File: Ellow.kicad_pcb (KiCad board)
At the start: 2 copper layers, 46 parts, among them J2 686116183422, J3 Conn_01x02_Female, Q1 A03407, Q2 A03407, SW9 RotaryEncoder_Switch, U1 AP2112K-3.3

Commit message: saved
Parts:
- added J1: USB_C_Receptacle_USB2.0, Connector_USB:USB_C_Receptacle_HRO_TYPE-C-31-M-12, F.Cu at (237.5, 92.7)
- added J4: Bus_M.2_Socket_A, ellow:M_2_EdgeConnector, F.Cu at (224.8, 102.9)
- added U2: E73-2G4M08S1C, ellow:E73-2G4M08S1C-52840, F.Cu at (237.5, 116.8)
- moved D1 23.6 mm to (163.8, 99.1)
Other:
- board outline added: 21 x 30 mm

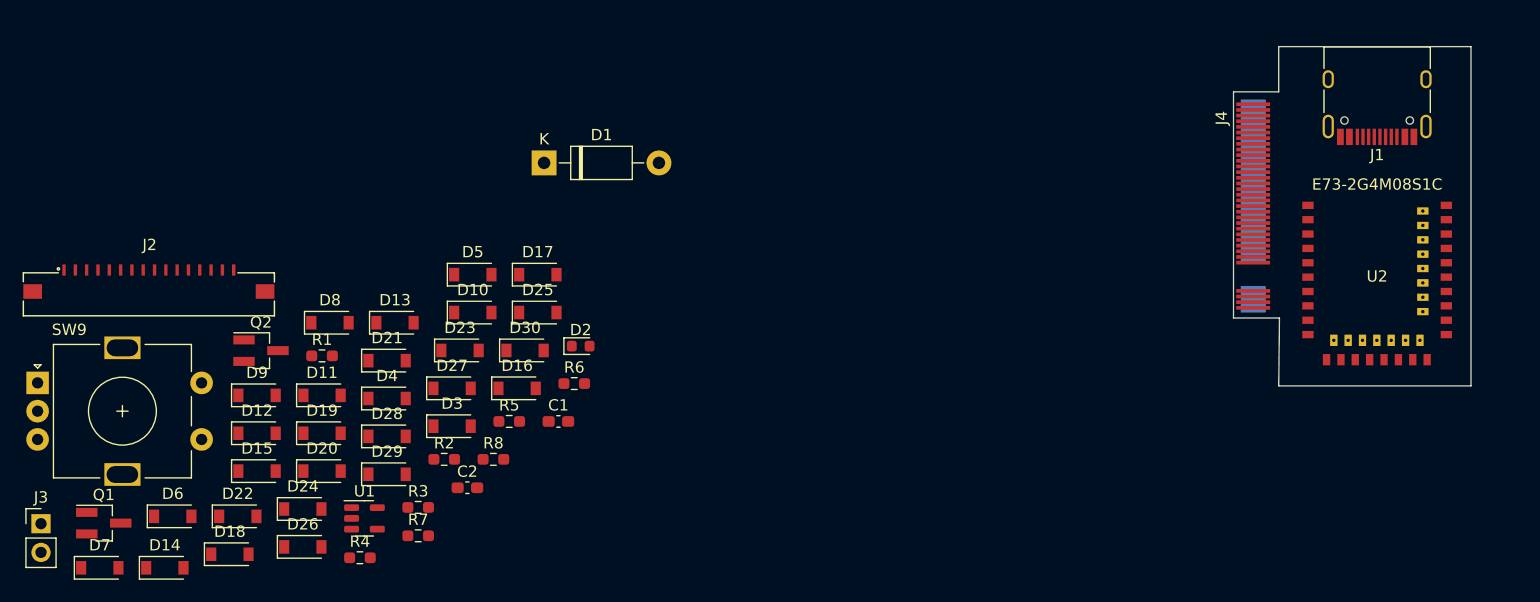
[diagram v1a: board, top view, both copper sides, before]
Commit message: moved shield stuff to another board
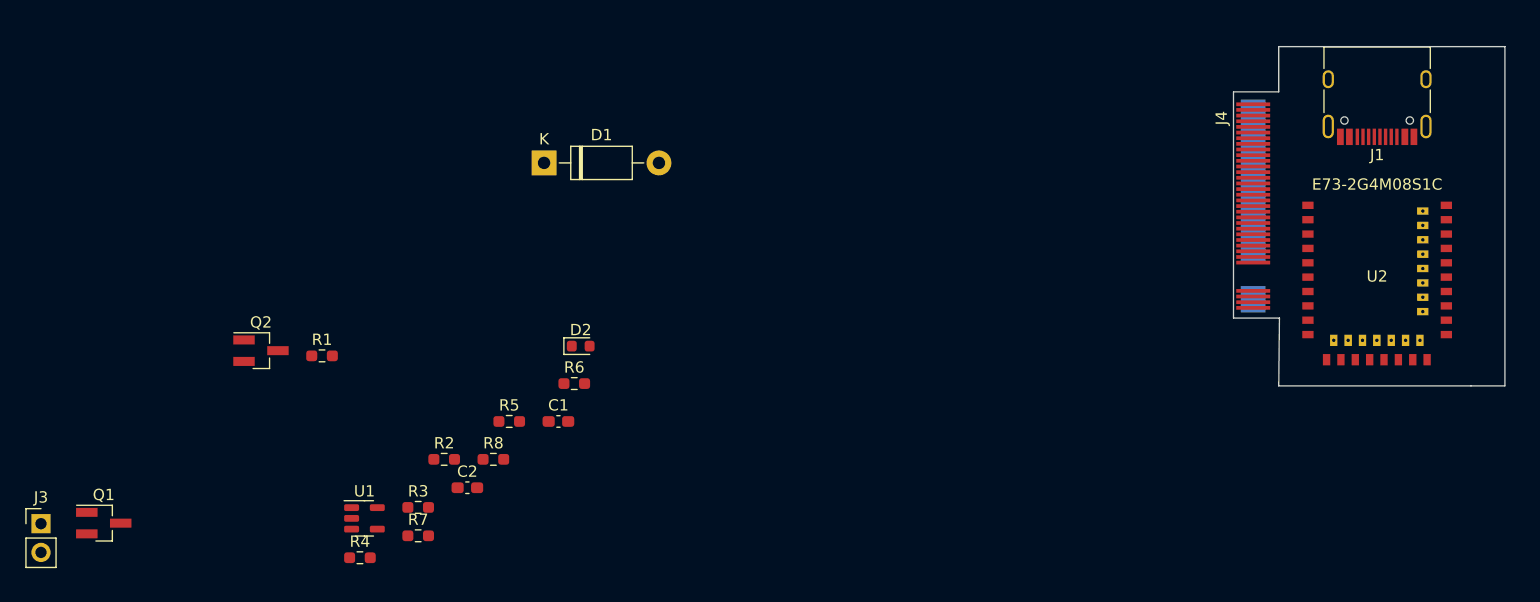
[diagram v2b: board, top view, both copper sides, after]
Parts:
- removed D10, D11, D12, D13, D14, D15, D16, D17, D18, D19, D20, D21, D22, D23, D24, D25, D26, D27, D28, D29, D3, D30, D4, D5, D6, D7, D8, D9: D_Small, Diode_SMD:D_SOD-123
- removed J2: 686116183422, 686116183422:686116183422
- removed SW9: RotaryEncoder_Switch, Rotary_Encoder:RotaryEncoder_Alps_EC11E-Switch_Vertical_H20mm
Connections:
- J4 pad 1: Net-(J4-Pad1) -> GND
- J4 pad 18: Net-(J4-Pad1) -> GND
- J4 pad 2: Net-(J4-Pad2) -> VDD_H
- J4 pad 23: Net-(J4-Pad1) -> GND
- J4 pad 24: Net-(J4-Pad1) -> GND
- J4 pad 29: Net-(J4-Pad1) -> GND
- J4 pad 30: Net-(J4-Pad1) -> GND
- J4 pad 33: Net-(J4-Pad1) -> GND
- J4 pad 36: Net-(J4-Pad1) -> GND
- J4 pad 39: Net-(J4-Pad1) -> GND
- J4 pad 4: Net-(J4-Pad2) -> VDD_H
- J4 pad 45: Net-(J4-Pad1) -> GND
- J4 pad 51: Net-(J4-Pad1) -> GND
- J4 pad 57: Net-(J4-Pad1) -> GND
- J4 pad 69: Net-(J4-Pad1) -> GND
- J4 pad 7: Net-(J4-Pad1) -> GND
- J4 pad 72: Net-(J4-Pad2) -> VDD_H
- J4 pad 74: Net-(J4-Pad2) -> VDD_H
- J4 pad 75: Net-(J4-Pad1) -> GND
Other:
- board size 21 x 30 mm -> 24 x 30 mm

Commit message: first board for quote check. not routed
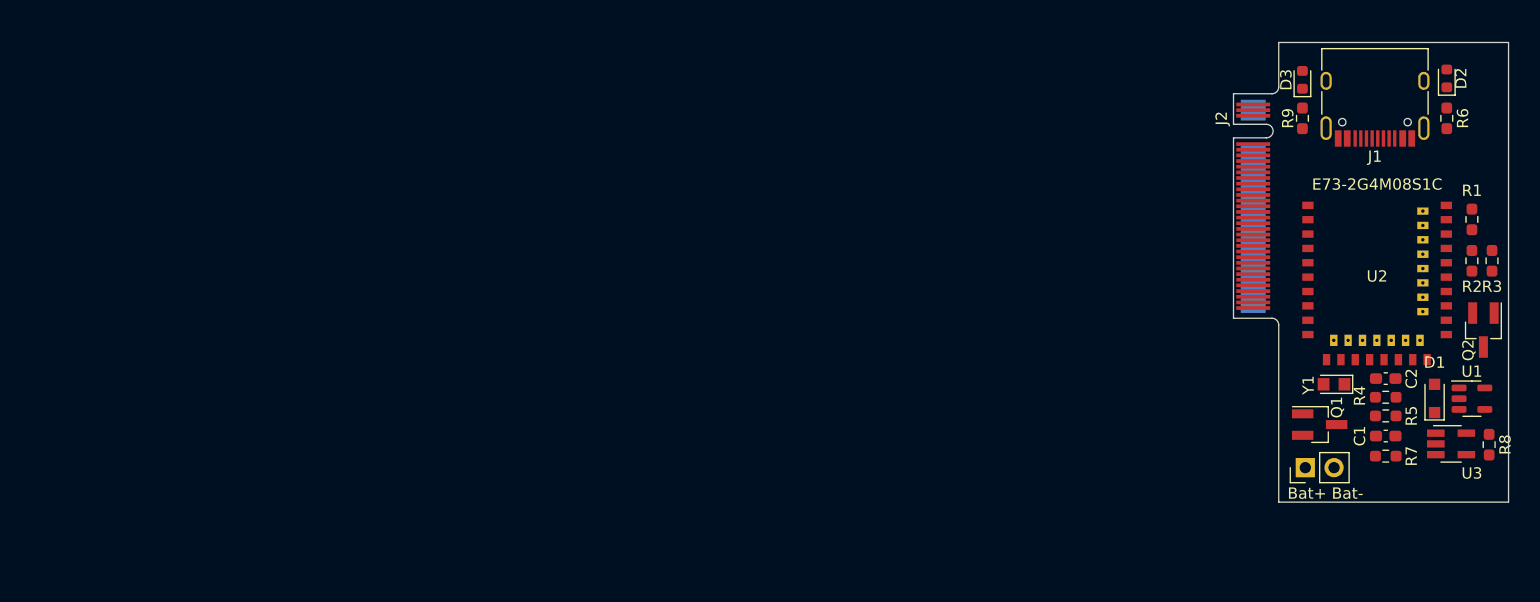
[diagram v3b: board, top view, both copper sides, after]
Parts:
- removed J4: Bus_M.2_Socket_A, ellow:M_2_EdgeConnector
- added D3: LED, LED_SMD:LED_0603_1608Metric, F.Cu at (230.9, 91.7)
- added J2: M_2_AKey_KB, ellow:M_2_EdgeConnector_A_Key, F.Cu at (224.8, 102.9)
- added R9: 10k, Resistor_SMD:R_0603_1608Metric_Pad0.98x0.95mm_HandSolder, F.Cu at (230.9, 95.1)
- added U3: LN2054Y42AMR, Package_TO_SOT_SMD:SOT-23-5_HandSoldering, F.Cu at (244.0, 123.9)
- added Y1: 32.768kHz, Crystal:Crystal_SMD_2012-2Pin_2.0x1.2mm_HandSoldering, F.Cu at (233.7, 118.6)
- Bat+ Bat-: renamed from J3
- D1: footprint Diode_THT:D_DO-41_SOD81_P10.16mm_Horizontal -> Diode_SMD:D_SOD-323_HandSoldering
- moved Bat+ Bat- 111.9 mm to (231.1, 126.0), turned to 90 degrees
- moved Q2 108.1 mm to (246.9, 113.8), turned to 270 degrees
- moved Q1 107.9 mm to (232.4, 122.2)
- moved R1 102.4 mm to (245.9, 104.1), turned to 90 degrees
- moved U1 98.5 mm to (245.9, 119.9)
- moved R3 97.4 mm to (247.7, 107.7), turned to 270 degrees
- moved R2 92.6 mm to (245.9, 107.7), turned to 90 degrees
- moved R4 91.8 mm to (238.3, 119.8), turned to 180 degrees
- moved R8 88.1 mm to (247.4, 124.0), turned to 270 degrees
- moved R7 85.8 mm to (238.3, 125.0)
- moved C2 81.8 mm to (238.3, 118.1), turned to 180 degrees
- moved D1 81.4 mm to (242.6, 119.9), turned to 90 degrees
- moved R6 80.6 mm to (243.6, 95.1), turned to 270 degrees
- moved D2 80.2 mm to (243.6, 91.6), turned to 90 degrees
- moved R5 77.5 mm to (238.3, 121.4)
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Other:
- board size 24 x 30 mm -> 24.3 x 40.6 mm

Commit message: starting to look at routing
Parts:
- added H1: MountingHole, ellow:MountingHole_M.2_3mm, F.Cu at (244.1, 107.2)
- C1: footprint Capacitor_SMD:C_0603_1608Metric_Pad1.08x0.95mm_HandSolder -> Capacitor_SMD:C_0603_1608Metric; moved to B.Cu
- C2: footprint Capacitor_SMD:C_0603_1608Metric_Pad1.08x0.95mm_HandSolder -> Capacitor_SMD:C_0603_1608Metric
- D1: footprint Diode_SMD:D_SOD-323_HandSoldering -> Diode_SMD:D_SOD-323
- J3: renamed from Bat+ Bat-; footprint Connector_PinHeader_2.54mm:PinHeader_1x02_P2.54mm_Vertical -> Connector_PinHeader_1.27mm:PinHeader_1x02_P1.27mm_Vertical
- Q1, Q2: footprint Package_TO_SOT_SMD:SOT-23_Handsoldering -> Package_TO_SOT_SMD:SOT-23
- R1, R2, R3, R8: moved to B.Cu
- U3: footprint Package_TO_SOT_SMD:SOT-23-5_HandSoldering -> Package_TO_SOT_SMD:SOT-23-5
- moved R8 28.0 mm to (233.9, 99.4), turned to 180 degrees
- moved U3 25.6 mm to (233.8, 100.5), turned to 270 degrees
- moved C1 23.7 mm to (240.8, 99.7)
- moved R7 21.5 mm to (240.8, 103.7)
- moved R3 19.8 mm to (236.0, 91.7), turned to 0 degrees
- moved U1 19.7 mm to (241.0, 100.8), turned to 90 degrees
- moved Q1 19.2 mm to (237.3, 103.7)
- moved D1 17.7 mm to (234.5, 104.2)
- moved Q2 16.7 mm to (237.4, 100.1)
- moved R2 16.3 mm to (236.0, 94.7), turned to 180 degrees
- moved R1 14.7 mm to (236.0, 93.2), turned to 0 degrees
- moved Y1 12.1 mm to (239.4, 107.9), turned to 0 degrees
- moved C2 12.1 mm to (226.8, 121.9)
- moved R5 11.7 mm to (226.9, 118.9), turned to 180 degrees
- moved R4 11.4 mm to (226.9, 120.4)
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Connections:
- net Net-(U2-Pad12) renamed P0.26
- net Net-(U2-Pad14) renamed P0.06
- net Net-(U2-Pad20) renamed P0.12
- net Net-(U2-Pad22) renamed 90.07
- net Net-(U2-Pad34) renamed P0.22
- net Net-(U2-Pad36) renamed P1.00
- net Net-(U2-Pad38) renamed P1.02
- net Net-(U2-Pad40) renamed P1.04
- J2 pad 1: (no net) -> GND
- J2 pad 16: (no net) -> P0.31
- J2 pad 17: (no net) -> P0.30
- J2 pad 18: (no net) -> Net-(J2-Pad18)
- J2 pad 19: (no net) -> Net-(J2-Pad19)
- J2 pad 2: (no net) -> EXT_VCC
- J2 pad 20: (no net) -> P0.29
- J2 pad 21: (no net) -> P0.02
- J2 pad 22: (no net) -> Net-(J2-Pad22)
- J2 pad 23: (no net) -> Net-(J2-Pad23)
- J2 pad 24: (no net) -> P1.13
- J2 pad 25: (no net) -> GND
- J2 pad 26: (no net) -> Net-(J2-Pad26)
- J2 pad 27: (no net) -> Net-(J2-Pad27)
- J2 pad 28: (no net) -> P0.03
- J2 pad 29: (no net) -> P0.28
- J2 pad 3: (no net) -> Net-(J2-Pad3)
- J2 pad 30: (no net) -> Net-(J2-Pad30)
- J2 pad 31: (no net) -> Net-(J2-Pad31)
- J2 pad 32: (no net) -> P1.11
- J2 pad 33: (no net) -> P1.06
- J2 pad 34: (no net) -> Net-(J2-Pad34)
- J2 pad 35: (no net) -> Net-(J2-Pad35)
- J2 pad 36: (no net) -> P0.10
- J2 pad 37: (no net) -> P0.09
- J2 pad 38: (no net) -> Net-(J2-Pad38)
- J2 pad 39: (no net) -> Net-(J2-Pad39)
- J2 pad 4: (no net) -> Net-(J2-Pad4)
- J2 pad 40: (no net) -> GND
- J2 pad 41: (no net) -> P0.24
- J2 pad 42: (no net) -> Net-(J2-Pad42)
- J2 pad 43: (no net) -> Net-(J2-Pad43)
- J2 pad 44: (no net) -> P0.13
- J2 pad 45: (no net) -> P0.20
- J2 pad 46: (no net) -> Net-(J2-Pad46)
- J2 pad 47: (no net) -> Net-(J2-Pad47)
- J2 pad 48: (no net) -> P0.17
- J2 pad 49: (no net) -> P0.15
- J2 pad 5: (no net) -> VBAT
- J2 pad 50: (no net) -> Net-(J2-Pad50)
- J2 pad 51: (no net) -> Net-(J2-Pad51)
- J2 pad 52: (no net) -> P0.08
- J2 pad 53: (no net) -> GND
- J2 pad 54: (no net) -> Net-(J2-Pad54)
- J2 pad 55: (no net) -> Net-(J2-Pad55)
- J2 pad 56: (no net) -> Net-(J2-Pad56)
- J2 pad 57: (no net) -> Net-(J2-Pad57)
- J2 pad 58: (no net) -> Net-(J2-Pad58)
- J2 pad 59: (no net) -> Net-(J2-Pad59)
- J2 pad 6: (no net) -> RESET
- J2 pad 60: (no net) -> Net-(J2-Pad60)
- J2 pad 61: (no net) -> Net-(J2-Pad61)
- J2 pad 62: (no net) -> Net-(J2-Pad62)
- J2 pad 63: (no net) -> Net-(J2-Pad63)
- J2 pad 64: (no net) -> Net-(J2-Pad64)
- J2 pad 65: (no net) -> Net-(J2-Pad65)
- J2 pad 66: (no net) -> DATA+
- J2 pad 67: (no net) -> DATA-
- J2 pad 68: (no net) -> Net-(J2-Pad68)
- J2 pad 69: (no net) -> Net-(J2-Pad69)
- J2 pad 7: (no net) -> Net-(J2-Pad7)
- J2 pad 70: (no net) -> SWD
- J2 pad 71: (no net) -> GND
- J2 pad 72: (no net) -> Net-(J2-Pad72)
- J2 pad 73: (no net) -> Net-(J2-Pad73)
- J2 pad 74: (no net) -> SWC
- J2 pad 75: (no net) -> VDD_H
- U2 pad 1: Net-(U2-Pad1) -> P1.11
- U2 pad 10: Net-(U2-Pad10) -> P0.30
- U2 pad 16: Net-(U2-Pad16) -> P0.08
- U2 pad 28: Net-(U2-Pad28) -> P0.15
- U2 pad 3: Net-(U2-Pad3) -> P0.03
- U2 pad 30: Net-(U2-Pad30) -> P0.17
- U2 pad 32: Net-(U2-Pad32) -> P0.20
- U2 pad 33: Net-(U2-Pad33) -> P0.13
- U2 pad 35: Net-(U2-Pad35) -> P0.24
- U2 pad 4: Net-(U2-Pad4) -> P0.28
- U2 pad 41: Net-(U2-Pad41) -> P0.09
- U2 pad 42: Net-(U2-Pad42) -> P1.06
- U2 pad 43: Net-(U2-Pad43) -> P0.10
- U2 pad 6: Net-(U2-Pad6) -> P1.13
- U2 pad 7: Net-(U2-Pad7) -> P0.02
- U2 pad 8: Net-(U2-Pad8) -> P0.29
- U2 pad 9: Net-(U2-Pad9) -> P0.31
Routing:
- added copper zone on B.Cu, net GND
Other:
- board size 24.3 x 40.6 mm -> 19.3 x 37.6 mm

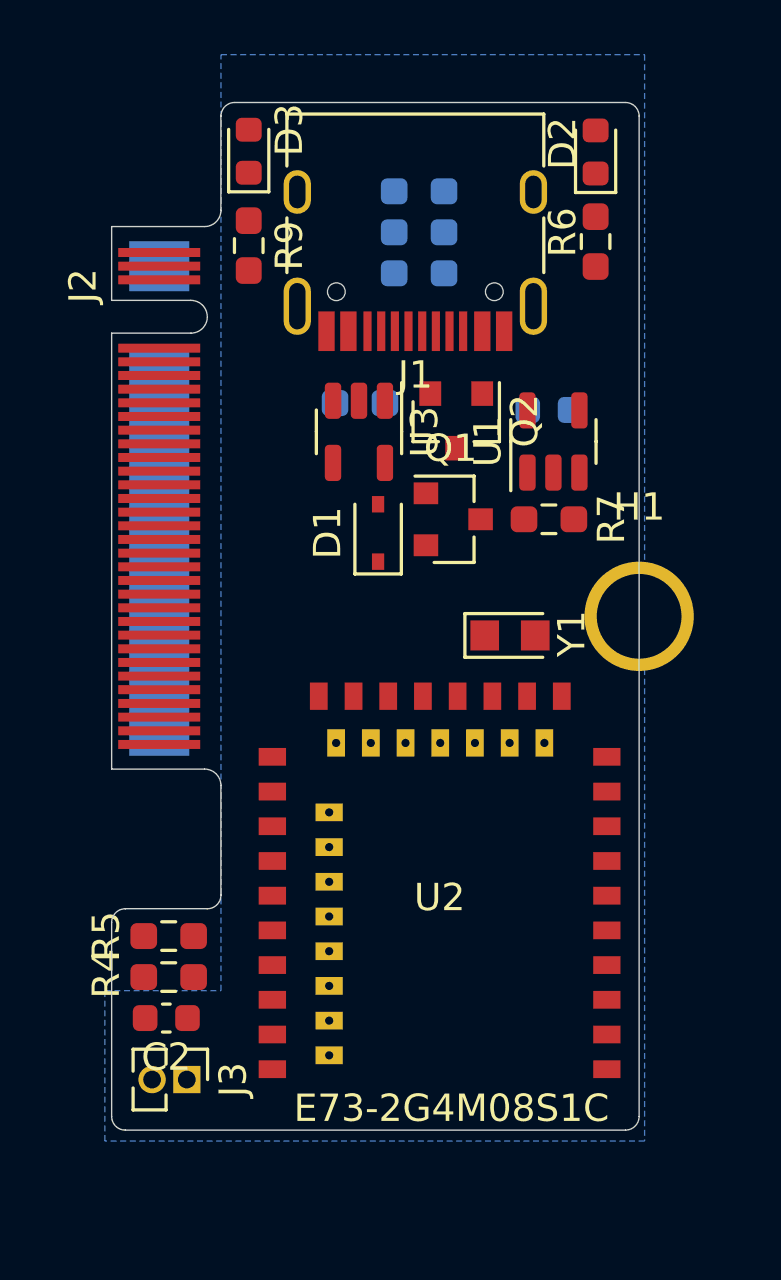
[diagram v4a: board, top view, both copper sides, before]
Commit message: no routing solution yet
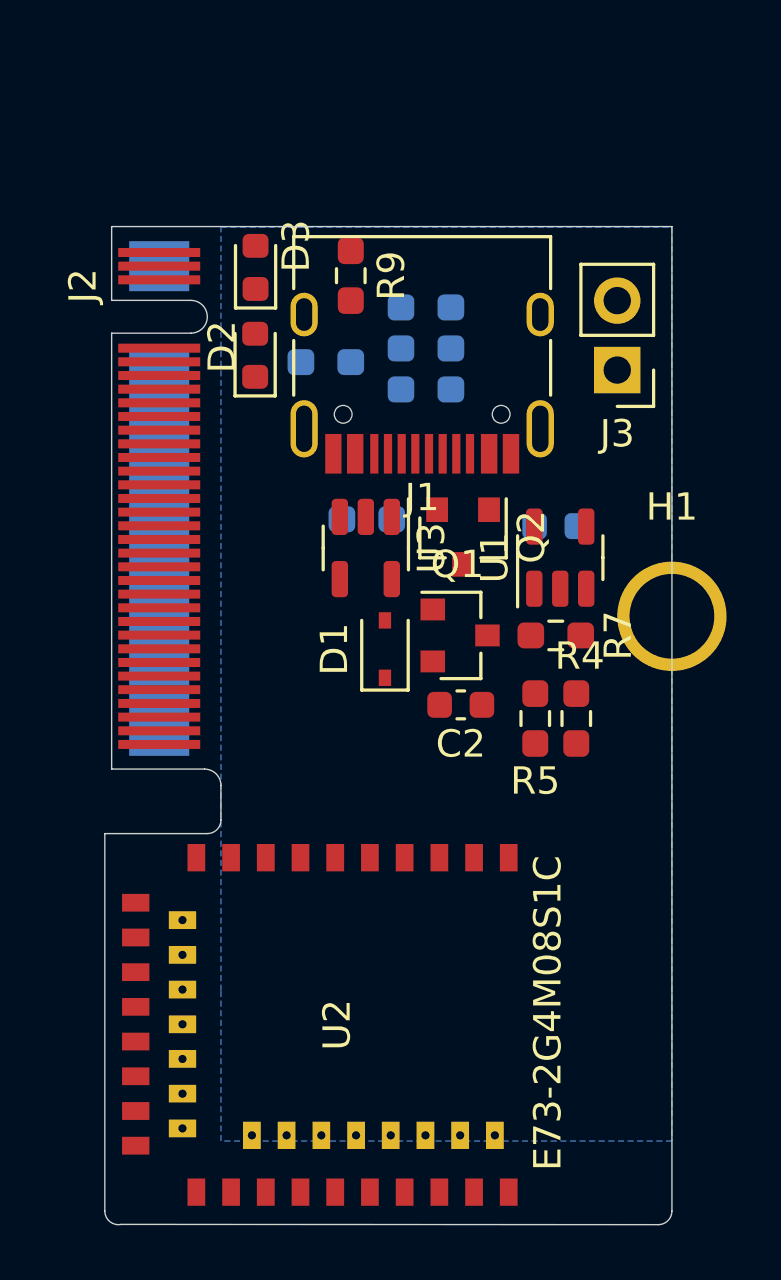
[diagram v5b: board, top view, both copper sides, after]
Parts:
- removed Y1: 32.768kHz, Crystal:Crystal_SMD_2012-2Pin_2.0x1.2mm_HandSoldering
- J3: footprint Connector_PinHeader_1.27mm:PinHeader_1x02_P1.27mm_Vertical -> Connector_PinHeader_2.54mm:PinHeader_1x02_P2.54mm_Vertical
- R6: moved to B.Cu
- moved J3 30.4 mm to (243.3, 98.2), turned to 180 degrees
- moved R4 17.7 mm to (241.8, 110.9), turned to 90 degrees
- moved U2 16.9 mm to (225.3, 122.2), turned to 0 degrees
- moved C2 15.7 mm to (237.6, 110.4)
- moved R5 15.6 mm to (240.3, 110.9), turned to 270 degrees
- moved D2 14.5 mm to (230.0, 97.7)
- moved R6 10.8 mm to (232.6, 97.9), turned to 0 degrees
- moved J1 4.49 mm to (236.2, 97.2)
- moved C1 4.26 mm to (241.0, 103.9)
- moved D1 4.26 mm to (234.8, 108.4)
- moved D3 4.26 mm to (230.1, 94.4)
- moved Q1 4.26 mm to (237.5, 107.9)
- moved Q2 4.26 mm to (237.6, 104.3)
- moved R1 4.26 mm to (236.3, 97.4)
- moved R2 4.26 mm to (236.3, 98.9)
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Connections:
- J2 pad 66: DATA+ -> Net-(J2-Pad66)
- J2 pad 67: DATA- -> Net-(J2-Pad67)
- J2 pad 70: SWD -> Net-(J2-Pad70)
- J2 pad 71: GND -> Net-(J2-Pad71)
- J2 pad 74: SWC -> Net-(J2-Pad74)
- J2 pad 75: VDD_H -> Net-(J2-Pad75)
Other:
- board size 19.3 x 37.6 mm -> 20.8 x 36.5 mm

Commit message: prelim routing
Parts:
- added J4: Conn_01x04_Female, ellow:PinHeader_1x04_P2.54mm_Vertical_small, F.Cu at (239.4, 127.1)
- added J5: Conn_01x04_Female, ellow:PinHeader_1x04_P2.54mm_Vertical_small, F.Cu at (236.4, 119.6)
- added Y1: 32.768kHz, Crystal:Crystal_SMD_2012-2Pin_2.0x1.2mm_HandSoldering, F.Cu at (241.3, 113.1)
- moved J2 16.5 mm to (225.3, 119.4)
- moved U2 14.7 mm to (237.8, 114.4), turned to 270 degrees
- moved C1 3.18 mm to (237.9, 104.6)
- moved C2 3.18 mm to (234.5, 111.1)
- moved D1 3.18 mm to (231.7, 109.1)
- moved Q1 3.18 mm to (234.4, 108.6)
- moved R7 3.18 mm to (237.9, 108.6)
- moved U1 3.18 mm to (238.1, 105.8)
- moved U3 3.18 mm to (231.0, 105.4)
- moved Q2 3.18 mm to (234.5, 105.0)
- moved R8 3.18 mm to (231.0, 104.4)
- moved R4 3.11 mm to (238.7, 111.1)
- moved R5 3.11 mm to (237.2, 111.1)
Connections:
- D3 pad 2: Net-(D3-Pad2) -> P0.07
- J2 pad 16: P0.31 -> GND
- J2 pad 17: P0.30 -> GND
- J2 pad 20: P0.29 -> Net-(J2-Pad20)
- J2 pad 21: P0.02 -> Net-(J2-Pad21)
- J2 pad 24: P1.13 -> Net-(J2-Pad24)
- J2 pad 25: GND -> Net-(J2-Pad25)
- J2 pad 28: P0.03 -> Net-(J2-Pad28)
- J2 pad 29: P0.28 -> Net-(J2-Pad29)
- J2 pad 32: P1.11 -> Net-(J2-Pad32)
- J2 pad 33: P1.06 -> Net-(J2-Pad33)
- J2 pad 36: P0.10 -> Net-(J2-Pad36)
- J2 pad 37: P0.09 -> Net-(J2-Pad37)
- J2 pad 40: GND -> Net-(J2-Pad40)
- J2 pad 41: P0.24 -> Net-(J2-Pad41)
- J2 pad 42: Net-(J2-Pad42) -> RESET
- J2 pad 44: P0.13 -> Net-(J2-Pad44)
- J2 pad 45: P0.20 -> Net-(J2-Pad45)
- J2 pad 47: Net-(J2-Pad47) -> P0.15
- J2 pad 48: P0.17 -> Net-(J2-Pad48)
- J2 pad 49: P0.15 -> Net-(J2-Pad49)
- J2 pad 51: Net-(J2-Pad51) -> P0.17
- J2 pad 52: P0.08 -> Net-(J2-Pad52)
- J2 pad 53: GND -> Net-(J2-Pad53)
- J2 pad 54: Net-(J2-Pad54) -> P0.13
- J2 pad 55: Net-(J2-Pad55) -> P0.20
- J2 pad 58: Net-(J2-Pad58) -> P0.24
- J2 pad 59: Net-(J2-Pad59) -> P0.22
- J2 pad 6: RESET -> Net-(J2-Pad6)
- J2 pad 63: Net-(J2-Pad63) -> P1.00
- J2 pad 67: Net-(J2-Pad67) -> P1.02
- J2 pad 70: Net-(J2-Pad70) -> P0.09
- J2 pad 71: Net-(J2-Pad71) -> P1.04
- J2 pad 74: Net-(J2-Pad74) -> P0.10
- J2 pad 75: Net-(J2-Pad75) -> P1.06
- U2 pad 10: P0.30 -> PROG
- U2 pad 15: PROG -> Net-(U2-Pad15)
- U2 pad 17: EXT_VCC_CONTROL -> Net-(U2-Pad17)
- U2 pad 18: BATTERY_MEASURE -> Net-(U2-Pad18)
- U2 pad 2: Net-(D3-Pad2) -> Net-(U2-Pad2)
- U2 pad 22: 90.07 -> P0.07
- U2 pad 8: P0.29 -> BATTERY_MEASURE
- U2 pad 9: P0.31 -> EXT_VCC_CONTROL
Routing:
- net VBUS: track 0.00 -> 55.3 mm, vias 0 -> 2
- net VBAT: track 0.00 -> 46.4 mm, vias 0 -> 2
- net DATA+: track 0.00 -> 46.2 mm, vias 0 -> 1
- net DATA-: track 0.00 -> 45.7 mm, vias 0 -> 1
- net VDD_H: track 0.00 -> 39.1 mm, vias 0 -> 1
- net P0.07: track 0.00 -> 33.8 mm, vias 0 -> 1
- net EXT_VCC_CONTROL: track 0.00 -> 20.7 mm
- net GND: track 0.00 -> 19.2 mm, vias 0 -> 5
- net Net-(C1-Pad1): track 0.00 -> 15.9 mm, vias 0 -> 2
- net BATTERY_MEASURE: track 0.00 -> 14.8 mm
- net EXT_VCC: track 0.00 -> 10.4 mm
- net Net-(D2-Pad2): track 0.00 -> 10.3 mm
- net P0.15: track 0.00 -> 7.78 mm
- net P0.17: track 0.00 -> 7.67 mm
- net P0.20: track 0.00 -> 7.56 mm
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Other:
- board size 20.8 x 36.5 mm -> 20.5 x 36.8 mm
